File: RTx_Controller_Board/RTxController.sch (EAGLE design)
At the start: 79 parts, among them U1 TPD4S014, X3 MINI-USB-32005-301

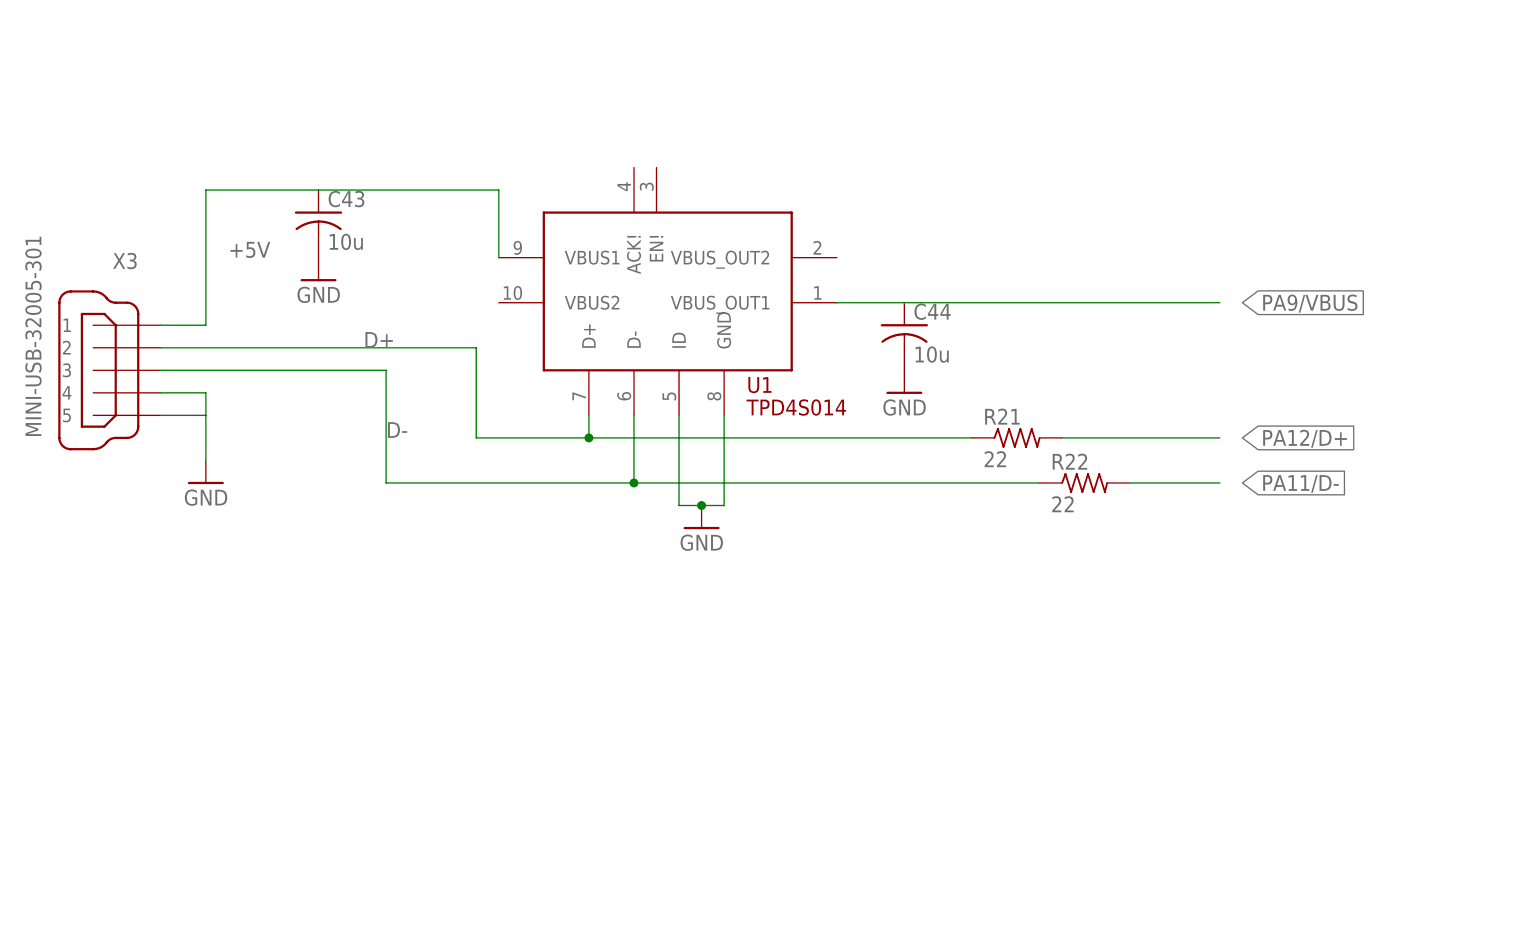
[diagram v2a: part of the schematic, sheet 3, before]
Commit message: Initial check-in of datasheet for USB ESD protection (better component selected). Updated USB in hardware to incorperate new esd chip.
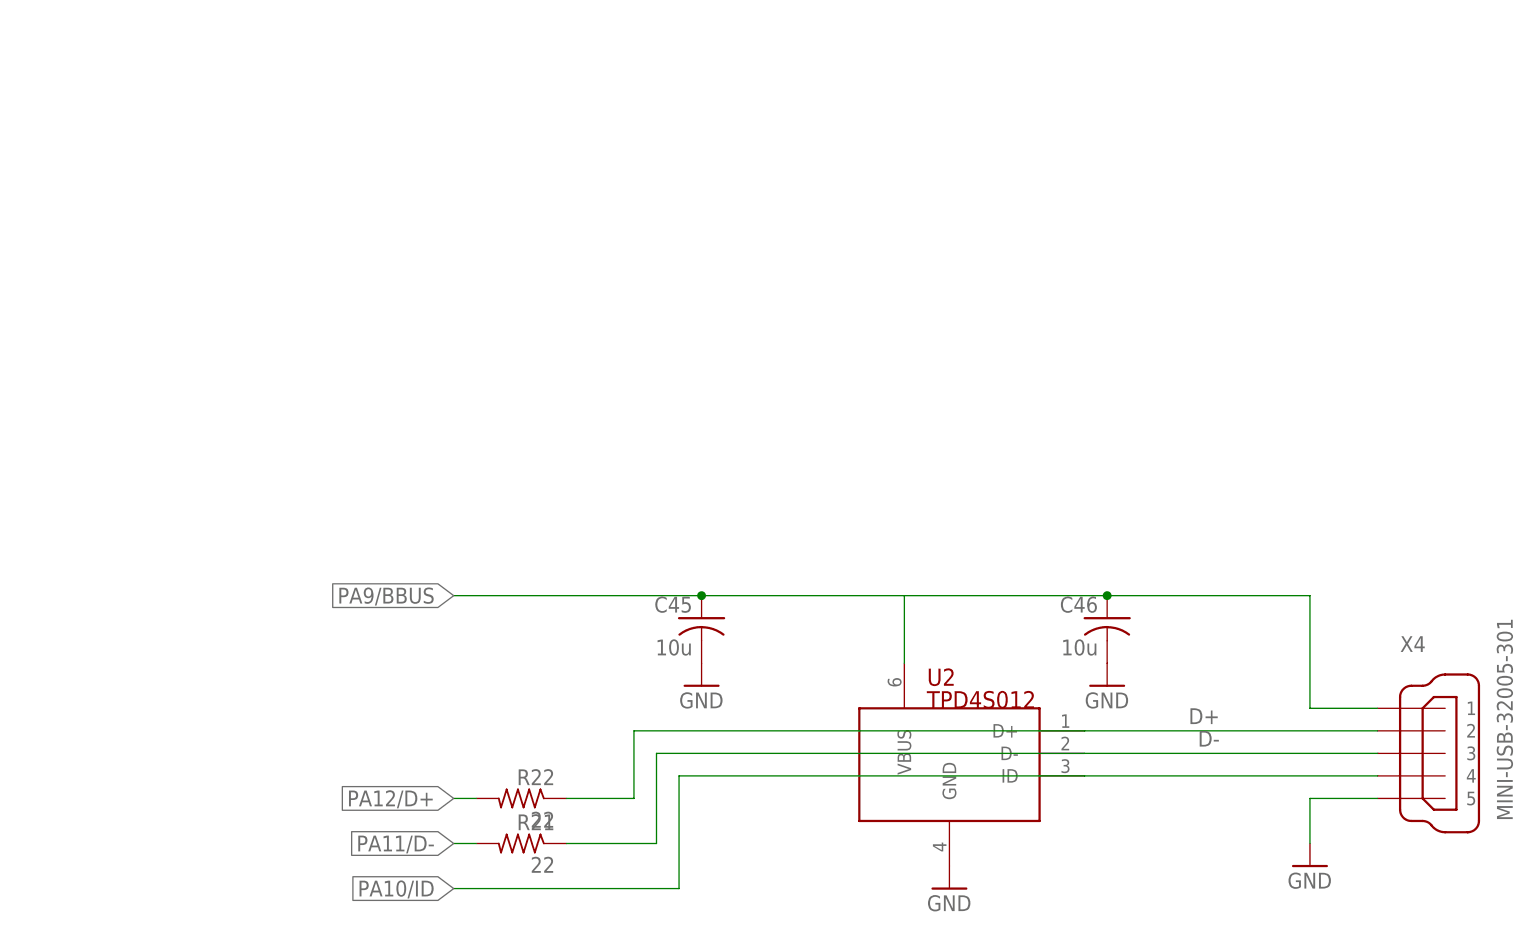
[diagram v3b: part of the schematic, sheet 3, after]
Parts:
- removed C43, C44: 10u, rcl:C-USC0402
- removed U1: TPD4S014, rtx:TPD4S014
- removed X3: MINI-USB-32005-301, con-cypressindustries:MINI-USB-32005-301
- added C45, C46: 10u, rcl:C-USC0402
- added U2: TPD4S012, rtx:TPD4S012
- added X4: MINI-USB-32005-301, con-cypressindustries:MINI-USB-32005-301
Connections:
- removed net PA9/VBUS: C44.1, U1.VBUS_OUT1
- new net PA10/ID: U2.ID, X4.4
- new net PA9/BBUS: C45.1, C46.1, U2.VBUS, X4.1
- net +5V: no longer C43.1, U1.VBUS1, X3.1
- net D+: now also R22.1, U2.D+, X4.2; no longer R21.1, U1.D+, X3.2
- net D-: now also R21.1, U2.D-, X4.3; no longer R22.1, U1.D-, X3.3
- net GND: now also C45.2, C46.2, U2.GND, X4.5; no longer C43.2, C44.2, U1.GND, U1.ID, X3.4, X3.5
- net PA11/D-: now also R21.2; no longer R22.2
- net PA12/D+: now also R22.2; no longer R21.2
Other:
- moved on the sheet: R21, R22

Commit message: Development of Ethernet PHY.
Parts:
- added C43, C47: 0.1uf 100v, motorFeedback:C-EUC0805K
- added C49: 0.1uf, motorFeedback:C-EUC0805K
- added D1: SMAJ58A, diode:SUPPRESSOR-SMBJ
- added D2: MMBD6050LT1SOT23, motorFeedback:MMBD6050LT1SOT23
- added F1: 1A, special:FUSE
- added IC1: LTC4263, motorFeedback:LTC4263
- added IC2: TLK110", motorFeedback:TLK110"
- added L1: 10mH, 21mA, motorFeedback:L-US0204V
- added LED1: (no value), motorFeedback:LED_HLMP-D101
- added R_LED: 1k, motorFeedback:R-US_R0603
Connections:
- new net 48VDC+: C43.1, D1.C, D2.C, F1.1, IC1.VDD48, LED1.A
- new net 48VDC-: C43.2, C49.2, IC1.LEGACY, IC1.MIDSPAN, IC1.OSC, IC1.PWRMGT, IC1.VSS, IC1.VSS@1
- new net N$15: C49.1, IC1.!SD!, IC1.ENFCLS, IC1.VDD5
- new net N$23: L1.2, LED1.C
- new net N$24: D2.A, L1.1, R_LED.2
- new net N$25: IC1.LED, R_LED.1
- new net PORT_MAGNETICS+: C47.1, F1.2
- new net PORT_MAGNETICS-: C47.2, D1.A, IC1.OUT, IC1.OUT@1
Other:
- note added: "Ethernet PHY"
- note added: "Isolated 48V Supply"

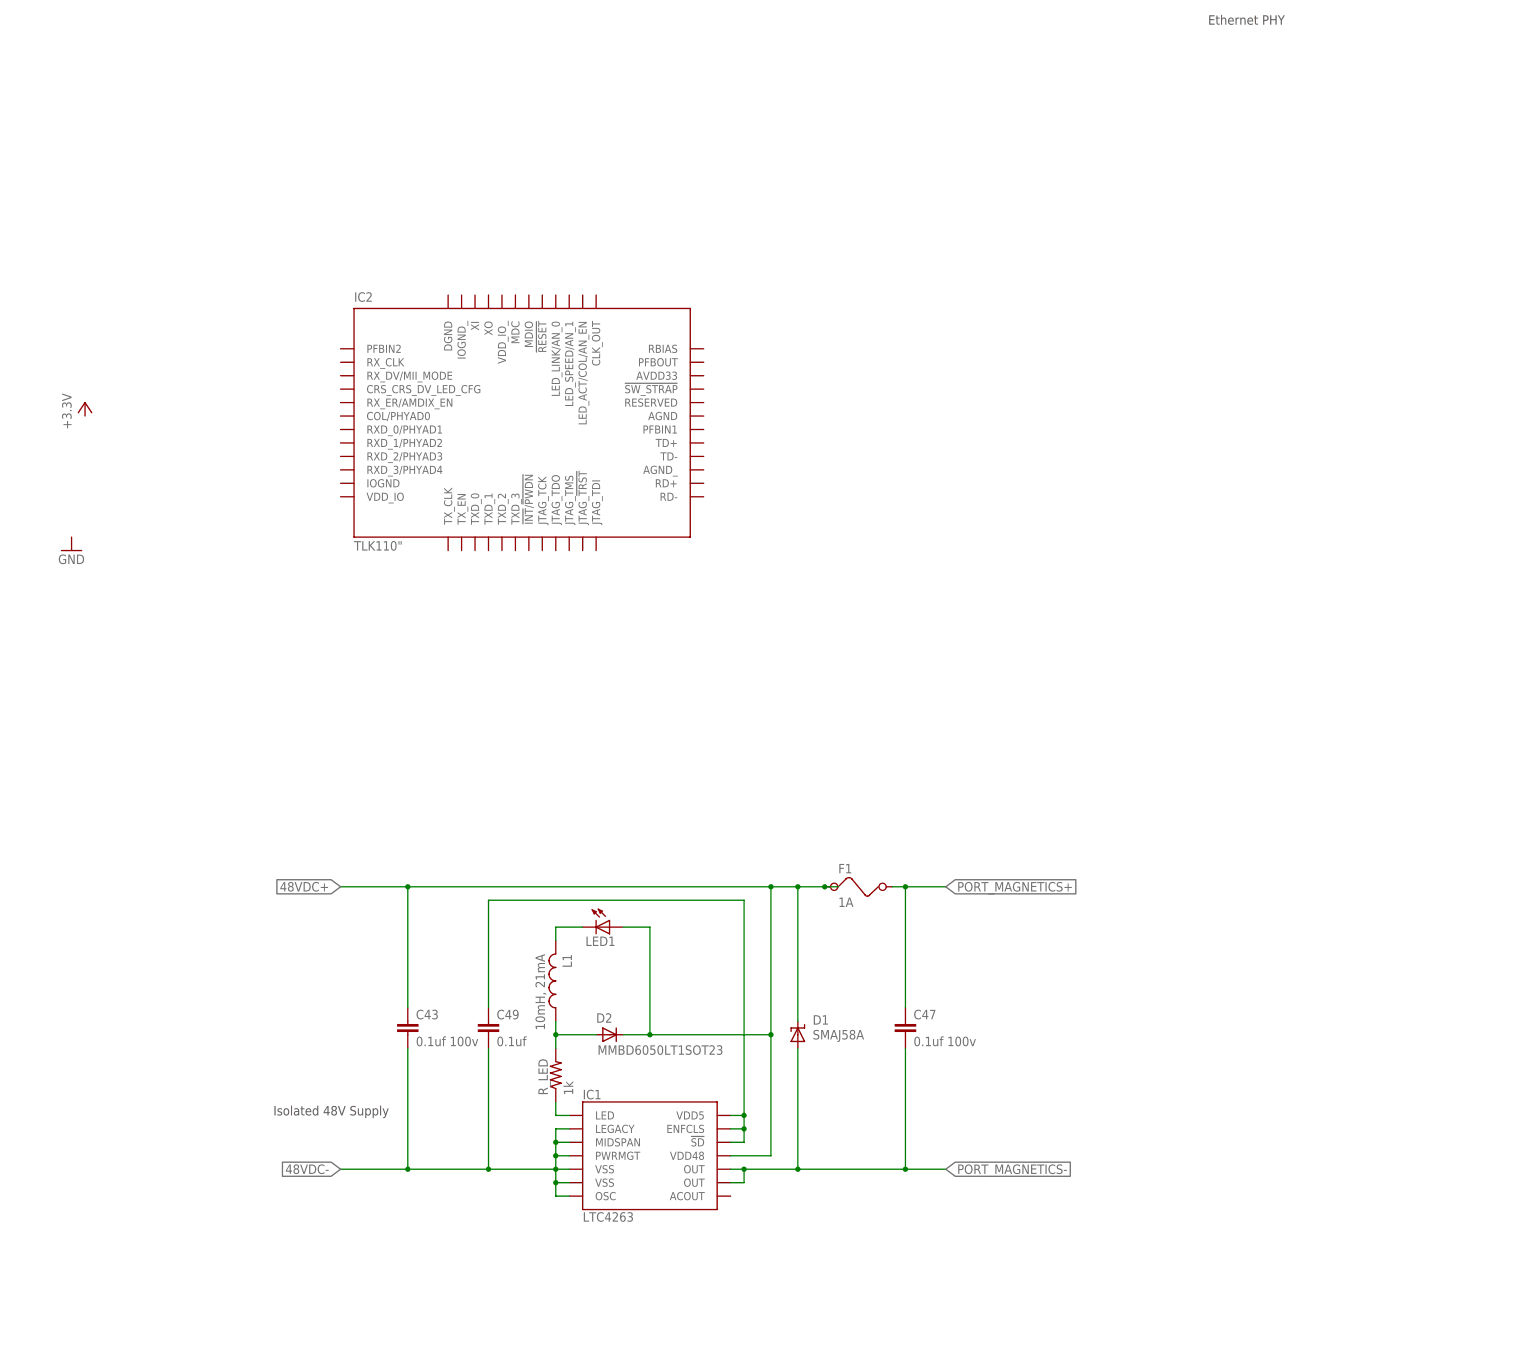
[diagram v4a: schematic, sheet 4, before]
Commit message: Added MagJack port to Eagle library.
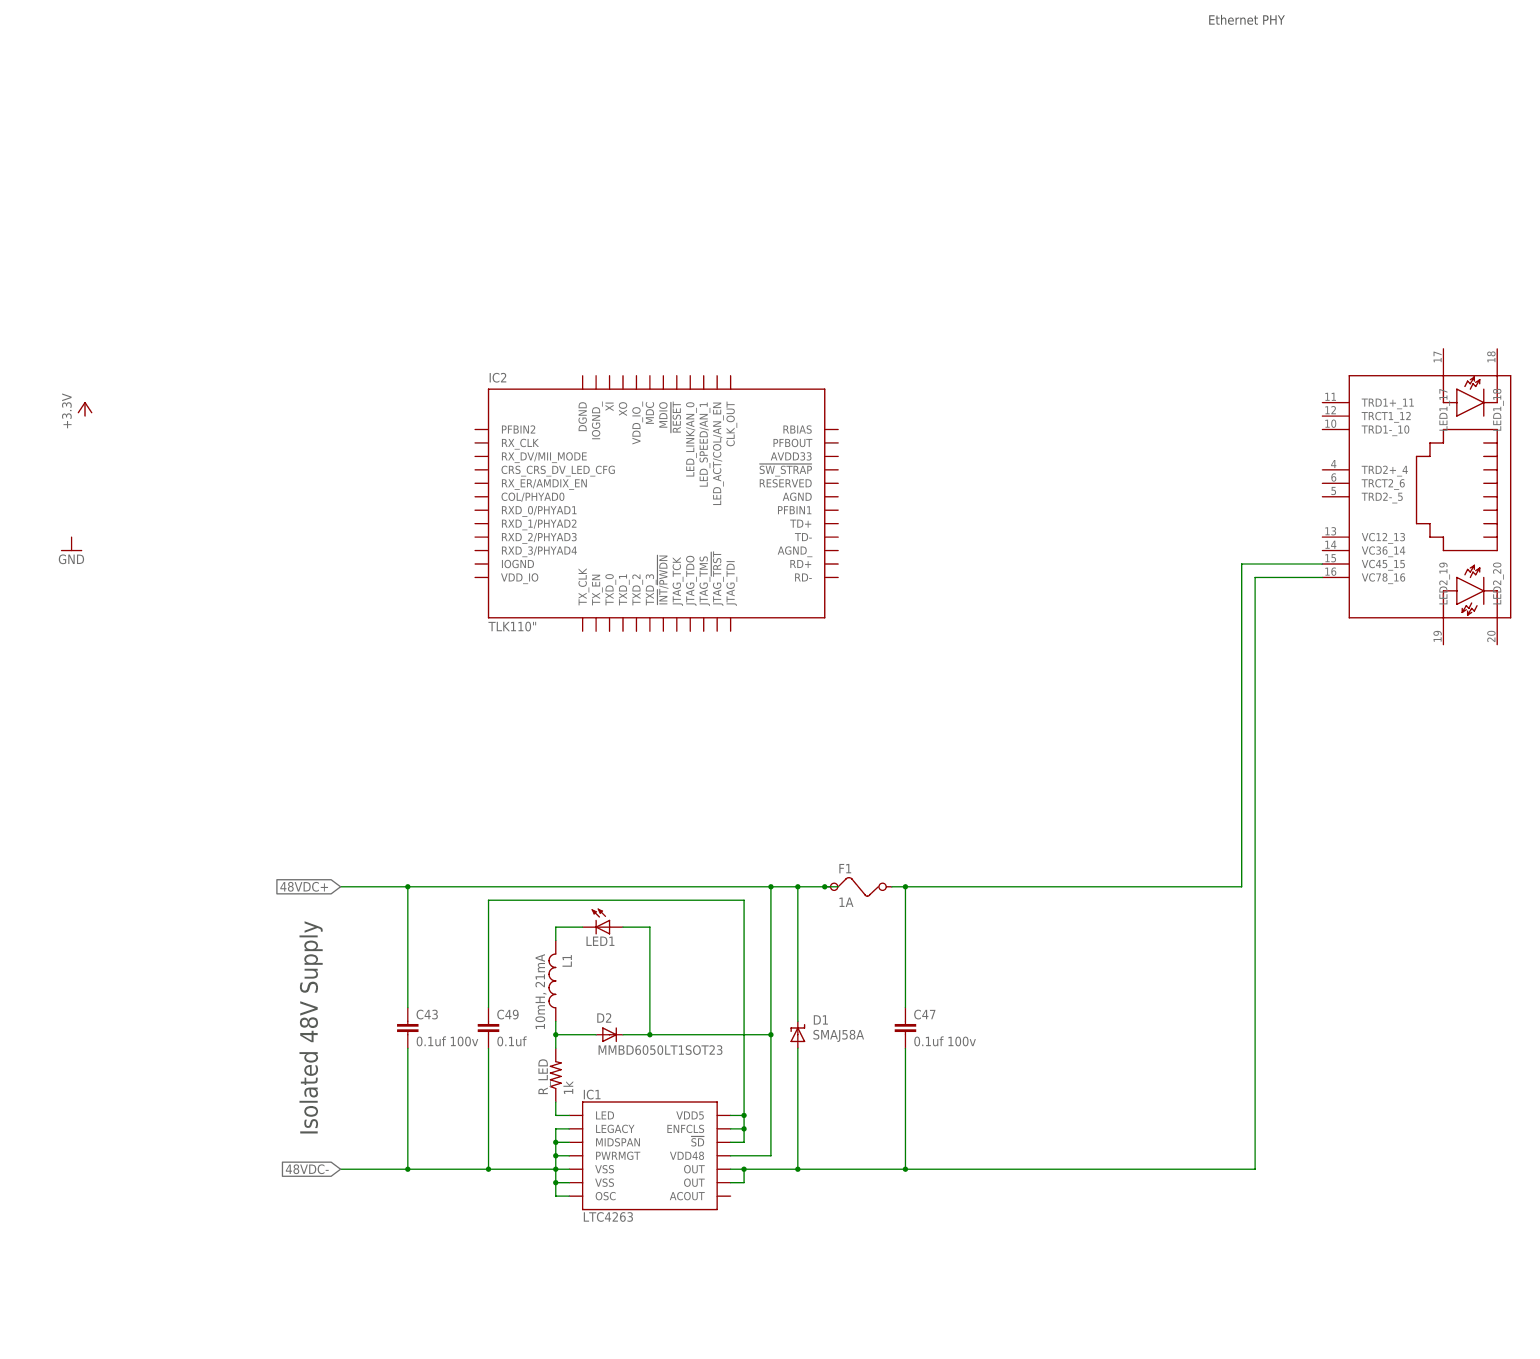
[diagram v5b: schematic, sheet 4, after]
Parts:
- added U$6: 0826-1X1T-GJ-F, motorFeedback:0826-1X1T-GJ-F
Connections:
- net PORT_MAGNETICS+: now also U$6.VC45_15
- net PORT_MAGNETICS-: now also U$6.VC78_16
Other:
- moved on the sheet: IC2
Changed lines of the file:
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@@
 <part name="D2" library="motorFeedback" deviceset="MMBD6050LT1" device="SOT23"/>
 <part name="C43" library="motorFeedback" deviceset="C-EU" device="C0805K" value="0.1uf 100v"/>
+<part name="U$6" library="motorFeedback" deviceset="0826-1X1T-GJ-F" device=""/>
 </parts>
 <sheets>
@@
 <plain>
 <text x="283.21" y="251.714" size="1.778" layer="97">Ethernet PHY</text>
-<text x="106.68" y="45.72" size="1.778" layer="97">Isolated 48V Supply</text>
+<text x="115.062" y="41.91" size="3.302" layer="97" rot="R90">Isolated 48V Supply</text>
 </plain>
 <instances>
 <instance part="U$5" gate="G$1" x="0" y="0"/>
 <instance part="IC1" gate="G$1" x="177.8" y="38.1"/>
-<instance part="IC2" gate="G$1" x="154.94" y="177.8"/>
+<instance part="IC2" gate="G$1" x="180.34" y="162.56"/>
 <instance part="D1" gate="G$1" x="205.74" y="60.96"/>
 <instance part="F1" gate="G$1" x="218.44" y="88.9"/>
@@
 <instance part="D2" gate="G$1" x="170.18" y="60.96"/>
 <instance part="C43" gate="G$1" x="132.08" y="63.5"/>
+<instance part="U$6" gate="G$1" x="325.12" y="165.1"/>
 </instances>
 <busses>
@@
 <junction x="205.74" y="35.56"/>
 <pinref part="C47" gate="G$1" pin="2"/>
-<wire x1="226.06" y1="35.56" x2="233.68" y2="35.56" width="0.1524" layer="91"/>
 <wire x1="226.06" y1="58.42" x2="226.06" y2="35.56" width="0.1524" layer="91"/>
 <junction x="226.06" y="35.56"/>
-<label x="233.68" y="35.56" size="1.778" layer="95" xref="yes"/>
+<wire x1="226.06" y1="35.56" x2="292.1" y2="35.56" width="0.1524" layer="91"/>
+<wire x1="292.1" y1="35.56" x2="292.1" y2="147.32" width="0.1524" layer="91"/>
+<pinref part="U$6" gate="G$1" pin="VC78_16"/>
+<wire x1="292.1" y1="147.32" x2="304.8" y2="147.32" width="0.1524" layer="91"/>
 </segment>
 </net>
@@
 <wire x1="223.52" y1="88.9" x2="226.06" y2="88.9" width="0.1524" layer="91"/>
 <pinref part="C47" gate="G$1" pin="1"/>
-<wire x1="226.06" y1="88.9" x2="233.68" y2="88.9" width="0.1524" layer="91"/>
 <wire x1="226.06" y1="66.04" x2="226.06" y2="88.9" width="0.1524" layer="91"/>
 <junction x="226.06" y="88.9"/>
-<label x="233.68" y="88.9" size="1.778" layer="95" xref="yes"/>
-</segment>
-</net>
+<wire x1="226.06" y1="88.9" x2="289.56" y2="88.9" width="0.1524" layer="91"/>
+<wire x1="289.56" y1="88.9" x2="289.56" y2="149.86" width="0.1524" layer="91"/>
+<pinref part="U$6" gate="G$1" pin="VC45_15"/>
+<wire x1="289.56" y1="149.86" x2="304.8" y2="149.86" width="0.1524" layer="91"/>
+</segment>
+</net>
